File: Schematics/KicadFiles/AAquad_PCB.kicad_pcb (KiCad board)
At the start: 2 copper layers, 55.6 x 48.8 mm, 47 parts, among them IC1 BMX160, IC2 MPL3115A2, IC3 levelShifter, IC4 levelShifter, IC5 levelShifter, IC6 levelShifter, J1 programmer, J2 Receiver_Output, J3 ESC_Input, J4 ultrasonic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

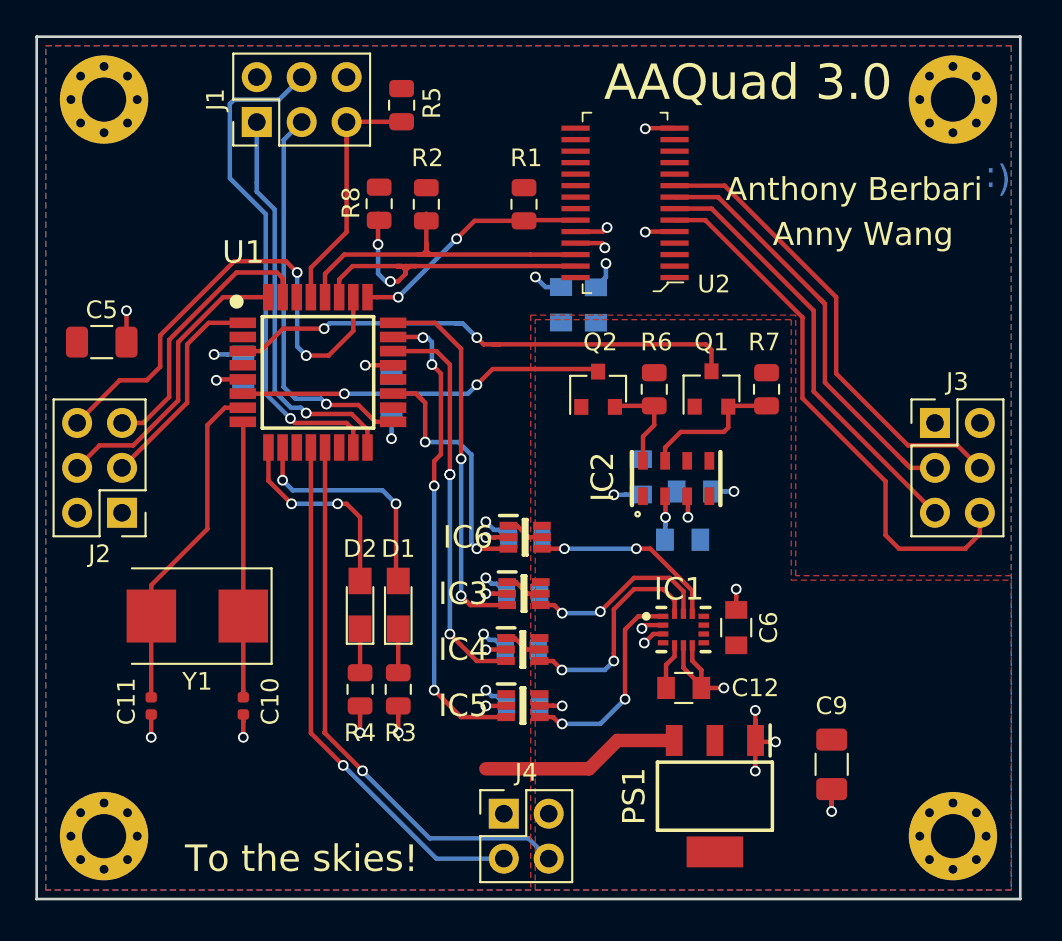
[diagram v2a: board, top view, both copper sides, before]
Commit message: Finished PCB Review. Sent out gerbers for manufacturing
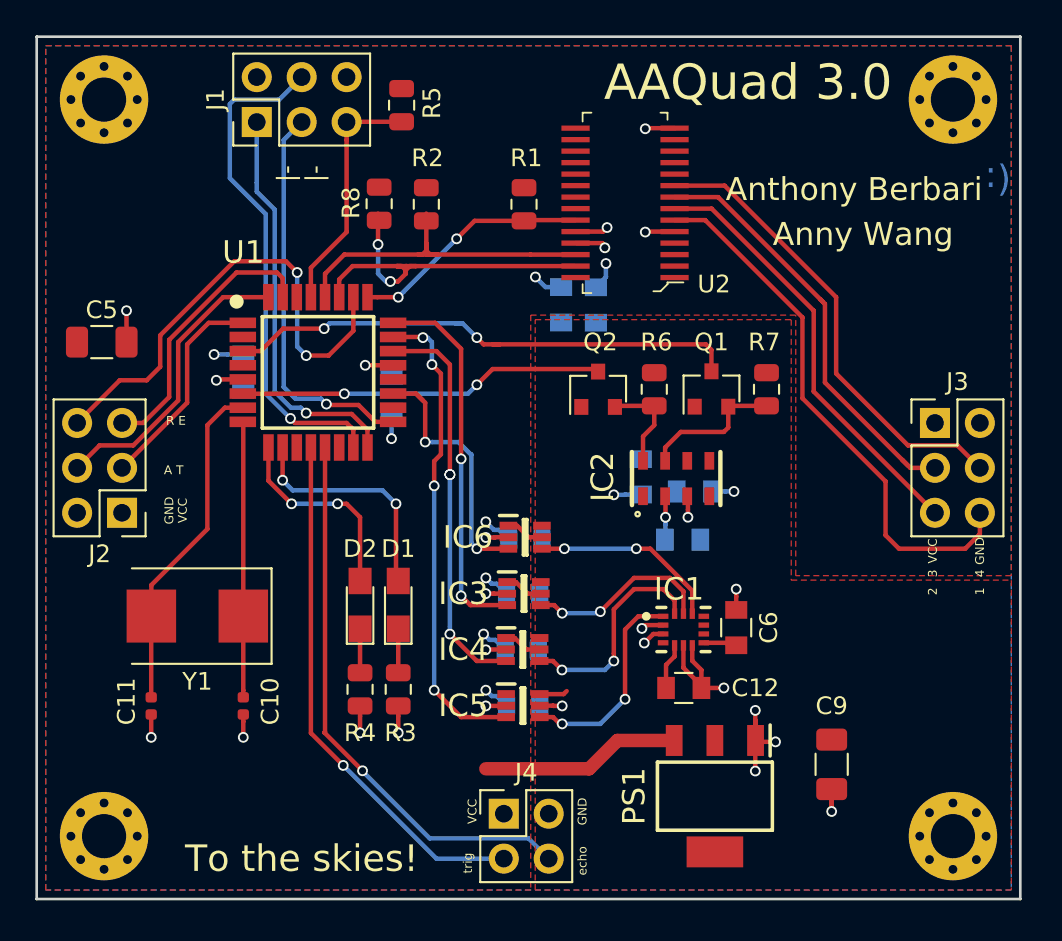
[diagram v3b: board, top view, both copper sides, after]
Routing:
- net VAA: track 5.37 -> 8.86 mm
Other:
- board text added: "-| -|"
- board text added: "1"
- board text added: "2"
- board text added: "3"
- board text added: "4"
- board text added: "A T"
- board text added: "GND"
- board text added: "R E"
- board text added: "To Freedom"
- board text added: "VCC"
- board text added: "echo"
- board text added: "trig"
- board text removed: "To Freedom !"
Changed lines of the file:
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@@
   (general
     (thickness 1.6)
-    (drawings 10)
-    (tracks 473)
+    (drawings 25)
+    (tracks 477)
     (zones 0)
     (modules 47)
@@
     (visible_elements 7FFFFFFF)
     (pcbplotparams
-      (layerselection 0x010e0_80000001)
+      (layerselection 0x010f0_ffffffff)
       (usegerberextensions false)
       (usegerberattributes false)
@@
       (psnegative false)
       (psa4output false)
-      (plotreference false)
-      (plotvalue true)
+      (plotreference true)
+      (plotvalue false)
       (plotinvisibletext false)
       (padsonsilk false)
@@
     (tags "capacitor 0805")
     (attr smd)
-    (fp_text reference C1 (at 0 1.5 270) (layer B.SilkS)
+    (fp_text reference C1 (at 0 1.778 270) (layer B.SilkS)
       (effects (font (size 1 1) (thickness 0.15)) (justify mirror))
     )
@@
     (pad 4 smd rect (at 3.15 0 270) (size 1.75 3.2) (layers F.Cu F.Paste F.Mask))
   )
+  (gr_text VCC (at 217.551 77.089 90) (layer F.SilkS)
+    (effects (font (size 0.5 0.5) (thickness 0.1)))
+  )
+  (gr_text GND (at 216.789 77.089 90) (layer F.SilkS)
+    (effects (font (size 0.5 0.5) (thickness 0.1)))
+  )
+  (gr_text 2 (at 259.969 81.661 90) (layer F.SilkS)
+    (effects (font (size 0.5 0.5) (thickness 0.1)))
+  )
+  (gr_text 1 (at 262.636 81.661 90) (layer F.SilkS)
+    (effects (font (size 0.5 0.5) (thickness 0.1)))
+  )
+  (gr_text 4 (at 262.636 80.645 90) (layer F.SilkS)
+    (effects (font (size 0.5 0.5) (thickness 0.1)))
+  )
+  (gr_text 3 (at 259.969 80.645 90) (layer F.SilkS)
+    (effects (font (size 0.5 0.5) (thickness 0.1)))
+  )
+  (gr_text GND (at 262.636 79.375 90) (layer F.SilkS)
+    (effects (font (size 0.5 0.5) (thickness 0.1)))
+  )
+  (gr_text VCC (at 259.969 79.375 90) (layer F.SilkS)
+    (effects (font (size 0.5 0.5) (thickness 0.1)))
+  )
+  (gr_text VCC (at 233.934 94.107 90) (layer F.SilkS)
+    (effects (font (size 0.5 0.5) (thickness 0.1)))
+  )
+  (gr_text GND (at 240.157 94.107 90) (layer F.SilkS)
+    (effects (font (size 0.5 0.5) (thickness 0.1)))
+  )
+  (gr_text echo (at 240.157 96.901 90) (layer F.SilkS)
+    (effects (font (size 0.5 0.5) (thickness 0.1)))
+  )
+  (gr_text trig (at 233.68 97.028 90) (layer F.SilkS)
+    (effects (font (size 0.5 0.5) (thickness 0.1)))
+  )
+  (gr_text "A T" (at 217.043 74.803) (layer F.SilkS)
+    (effects (font (size 0.5 0.5) (thickness 0.1)))
+  )
+  (gr_text "R E" (at 217.17 72.009) (layer F.SilkS)
+    (effects (font (size 0.5 0.5) (thickness 0.1)))
+  )
+  (gr_text "-|\n-|" (at 224.409 58.039 270) (layer F.SilkS)
+    (effects (font (size 1 1) (thickness 0.2)))
+  )
   (gr_text ":)" (at 263.652 58.42 180) (layer B.Cu)
     (effects (font (size 1.5 1.5) (thickness 0.3)) (justify mirror))
   )
-  (gr_text "To Freedom !" (at 247.142 53.594) (layer B.SilkS)
+  (gr_text "To Freedom" (at 247.142 53.594) (layer B.SilkS)
     (effects (font (size 2 2) (thickness 0.3)) (justify mirror))
   )
@@
   (segment (start 254.254 92.843) (end 254.254 93.853) (width 0.254) (layer F.Cu) (net 1) (status 10))
   (segment (start 254.254 94.107) (end 254.254 92.843) (width 0.254) (layer F.Cu) (net 1) (status 20))
-  (segment (start 236.335 84.298) (end 235.839 84.298) (width 0.254) (layer F.Cu) (net 2) (status 30))
-  (segment (start 236.985 84.948) (end 236.335 84.298) (width 0.254) (layer F.Cu) (net 2) (status 20))
-  (segment (start 237.739 84.948) (end 236.985 84.948) (width 0.254) (layer F.Cu) (net 2) (status 10))
-  (segment (start 236.401 81.138) (end 235.905 81.138) (width 0.254) (layer F.Cu) (net 2) (status 30))
-  (segment (start 237.051 81.788) (end 236.401 81.138) (width 0.254) (layer F.Cu) (net 2) (status 20))
-  (segment (start 237.805 81.788) (end 237.051 81.788) (width 0.254) (layer F.Cu) (net 2) (status 10))
-  (segment (start 236.467 77.948) (end 235.971 77.948) (width 0.254) (layer F.Cu) (net 2) (status 30))
-  (segment (start 237.117 78.598) (end 236.467 77.948) (width 0.254) (layer F.Cu) (net 2) (status 20))
-  (segment (start 237.871 78.598) (end 237.117 78.598) (width 0.254) (layer F.Cu) (net 2) (status 10))
-  (segment (start 244.888 76.293) (end 244.876 76.281) (width 0.254) (layer F.Cu) (net 8) (status 30))
   (segment (start 227.584 88.138) (end 227.584 88.7255) (width 0.254) (layer F.Cu) (net 1) (status 10))
   (via (at 227.584 89.662) (size 0.6096) (drill 0.4) (layers F.Cu B.Cu) (net 1))
@@
   (segment (start 214.376 67.564) (end 214.376 65.786) (width 0.254) (layer F.Cu) (net 1) (status 10))
   (via (at 214.376 65.786) (size 0.6096) (drill 0.4) (layers F.Cu B.Cu) (net 1))
+  (segment (start 236.335 84.298) (end 235.839 84.298) (width 0.254) (layer F.Cu) (net 2) (status 30))
+  (segment (start 236.985 84.948) (end 236.335 84.298) (width 0.254) (layer F.Cu) (net 2) (status 20))
+  (segment (start 237.739 84.948) (end 236.985 84.948) (width 0.254) (layer F.Cu) (net 2) (status 10))
+  (segment (start 236.401 81.138) (end 235.905 81.138) (width 0.254) (layer F.Cu) (net 2) (status 30))
+  (segment (start 237.051 81.788) (end 236.401 81.138) (width 0.254) (layer F.Cu) (net 2) (status 20))
+  (segment (start 237.805 81.788) (end 237.051 81.788) (width 0.254) (layer F.Cu) (net 2) (status 10))
+  (segment (start 236.467 77.948) (end 235.971 77.948) (width 0.254) (layer F.Cu) (net 2) (status 30))
+  (segment (start 237.117 78.598) (end 236.467 77.948) (width 0.254) (layer F.Cu) (net 2) (status 20))
+  (segment (start 237.871 78.598) (end 237.117 78.598) (width 0.254) (layer F.Cu) (net 2) (status 10))
   (segment (start 235.312763 87.581763) (end 235.028763 87.581763) (width 0.254) (layer B.Cu) (net 2))
   (segment (start 235.869 88.138) (end 235.312763 87.581763) (width 0.254) (layer B.Cu) (net 2) (status 10))
@@
   (segment (start 244.888 85.82) (end 244.888 87.122) (width 0.254) (layer F.Cu) (net 5) (status 20))
   (segment (start 245.372 85.336) (end 244.888 85.82) (width 0.254) (layer F.Cu) (net 5))
+  (segment (start 248.7175 84.57) (end 248.8565 84.709) (width 0.254) (layer F.Cu) (net 5))
+  (segment (start 247.022 84.57) (end 248.7175 84.57) (width 0.254) (layer F.Cu) (net 5))
+  (segment (start 237.744 87.473) (end 239.0948 87.473) (width 0.254) (layer F.Cu) (net 5))
+  (segment (start 239.0948 87.473) (end 239.268 87.2998) (width 0.254) (layer F.Cu) (net 5))
   (segment (start 220.98 72.101) (end 220.953 72.074) (width 0.254) (layer F.Cu) (net 6) (status 30))
   (segment (start 220.98 83.058) (end 220.98 72.101) (width 0.254) (layer F.Cu) (net 6) (status 30))
@@
   (segment (start 215.773 83.065) (end 215.78 83.058) (width 0.254) (layer F.Cu) (net 7) (status 30))
   (segment (start 215.773 87.653) (end 215.773 83.065) (width 0.254) (layer F.Cu) (net 7) (status 30))
+  (segment (start 244.888 76.293) (end 244.876 76.281) (width 0.254) (layer F.Cu) (net 8) (status 30))
   (segment (start 244.856 76.301) (end 244.876 76.281) (width 0.254) (layer F.Cu) (net 8) (status 30))
   (segment (start 244.856 78.74) (end 244.856 77.861) (width 0.254) (layer B.Cu) (net 8) (status 10))
